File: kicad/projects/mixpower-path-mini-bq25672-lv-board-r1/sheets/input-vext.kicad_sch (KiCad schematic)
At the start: 7 parts, among them J4 VEXT, Q5 SIA931DJ

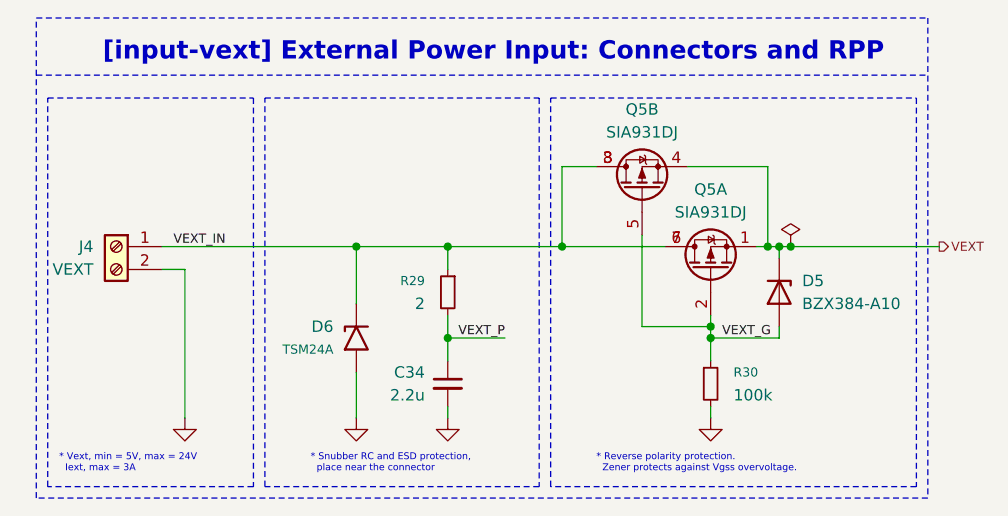
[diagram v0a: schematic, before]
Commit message: feat: generate schematic PDF and fix minor schematic mistakes
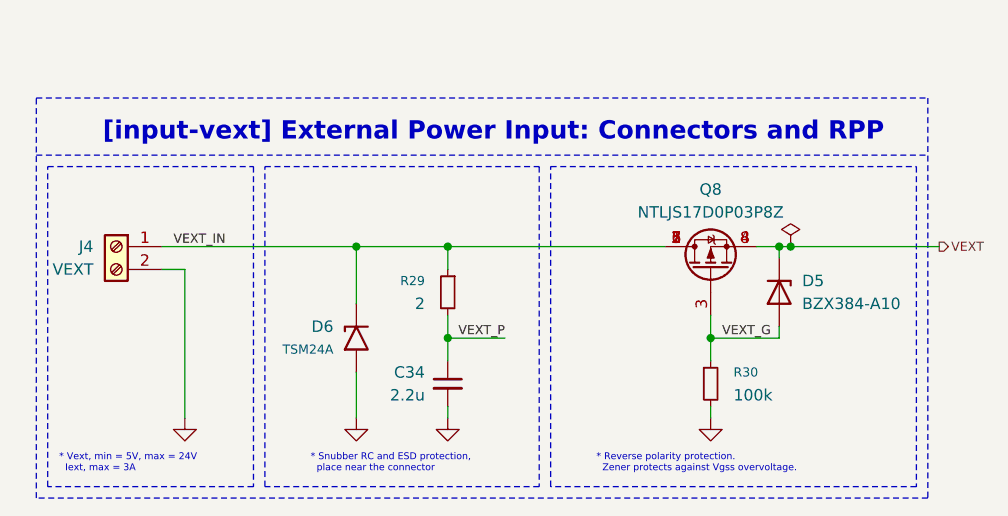
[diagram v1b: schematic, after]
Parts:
- removed Q5: SIA931DJ, mixlib-generic-dfn:Diodes-Incorporated_U-DFN2020-6_Type-B, symbol mixlib-discrete-mosfet:SIA931DJ
- added Q8: NTLJS17D0P03P8Z, mixlib-vendor-onsemi:vendor-onsemi-483av, symbol mixlib-discrete-mosfet:NTLJS17D0P03P8Z
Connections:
- net VEXT: now also Q8.4 (S), Q8.8 (S)
- net VEXT_G: now also Q8.3 (G)
- net VEXT_IN: now also Q8.1 (D), Q8.2 (D), Q8.5 (D), Q8.6 (D), Q8.7 (D)

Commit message: feat: small changes in schematics, some PCB routing
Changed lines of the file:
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@@
 		(lib_id "Device:R_Small")
 		(at 113.03 63.5 0)
-		(mirror y)
 		(unit 1)
 		(exclude_from_sim no)
@@
 		(dnp no)
 		(property "Reference" "R29"
-			(at 110.49 62.2299 0)
+			(at 115.57 62.2299 0)
 			(effects
 				(font
@@
 		)
 		(property "Value" "2"
-			(at 110.49 64.7699 0)
+			(at 115.57 64.7699 0)
 			(effects
 				(font
@@
 		)
 		(instances
-			(project ""
+			(project "mixpower-path-mini-bq25672-lv-board-r1"
 				(path "/2e43857b-9bf9-460c-948c-ec2cf8a8d6b4/050b3b40-3e43-4f8a-9f9d-8e85b6cb1fd2"
 					(reference "J4")
@@
 		)
 		(instances
-			(project ""
+			(project "mixpower-path-mini-bq25672-lv-board-r1"
 				(path "/2e43857b-9bf9-460c-948c-ec2cf8a8d6b4/050b3b40-3e43-4f8a-9f9d-8e85b6cb1fd2"
 					(reference "D5")
@@
 		)
 		(instances
-			(project ""
+			(project "mixpower-path-mini-bq25672-lv-board-r1"
 				(path "/2e43857b-9bf9-460c-948c-ec2cf8a8d6b4/050b3b40-3e43-4f8a-9f9d-8e85b6cb1fd2"
 					(reference "D6")
@@
 		)
 		(instances
-			(project ""
+			(project "mixpower-path-mini-bq25672-lv-board-r1"
 				(path "/2e43857b-9bf9-460c-948c-ec2cf8a8d6b4/050b3b40-3e43-4f8a-9f9d-8e85b6cb1fd2"
 					(reference "Q8")

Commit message: feat: failed PCB routing
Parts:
- removed D5: BZX384-A10, Diode_SMD:D_SOD-323, symbol Diode:BZX384xxxx
- removed D6: TSM24A, Package_TO_SOT_SMD:SOT-23, symbol Diode:TSM24A
- added C13: 10u, Capacitor_SMD:C_0402_1005Metric, symbol Device:C_Small
- added D2: PESD24VV1BA, Diode_SMD:D_SOD-323, symbol Device:D_TVS_Small
- added D3: BZX584C18, Diode_SMD:D_SOD-523, symbol Diode:DZ2S180X0L
- C12: renamed from C34; footprint Capacitor_SMD:C_0603_1608Metric -> Resistor_SMD:R_0402_1005Metric
- renumbered J4 to J5, Q8 to Q4, R29 to R22, R30 to R23
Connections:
- net GND: now also C13.2, D2.1 (A1)
- net VEXT: now also C13.1, D3.1 (K)
- net VEXT_G: now also D3.2 (A)
- net VEXT_IN: now also D2.2 (A2)
- net VEXT_P renamed VEXT_FLT_P
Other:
- moved on the sheet: Q4, R23
